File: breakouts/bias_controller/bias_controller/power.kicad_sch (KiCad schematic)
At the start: 9 parts, among them U7 LM2776

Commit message: top level schematic work
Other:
- note added: "add a few LEDs"
- moved on the sheet: C22, C23, C24, U7

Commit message: more bias controller schematic work
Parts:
- added C42, C43, C44: 4.7 uF, symbol Device:C_Small
- added R68: 20k, symbol Device:R_Small
- added R69: 0, symbol Device:R_Small
- added U18: LT3094xMSE, Package_SO:MSOP-12-1EP_3x4mm_P0.65mm_EP1.65x2.85mm, symbol Regulator_Linear:LT3094xMSE
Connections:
- net -6V: now also C42.1, U18.1 (IN), U18.13 (IN), U18.2 (IN), U18.3 (EN/UV), U18.5 (PGFB)
- net GND: now also C42.2, C43.2, C44.2, R68.1, U18.9 (GND)
- net VSS: now also C43.1, C44.1, R69.2, U18.10 (OUTS), U18.11 (OUT), U18.12 (OUT); no longer C25.1
- new net: R68.2, U18.6 (ILIM)
- new net VSS_EXT: C25.1, R69.1
- no-connect marks 0 -> 2
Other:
- note removed: "add negative ldo"
- moved on the sheet: C25, C26, R25, R26

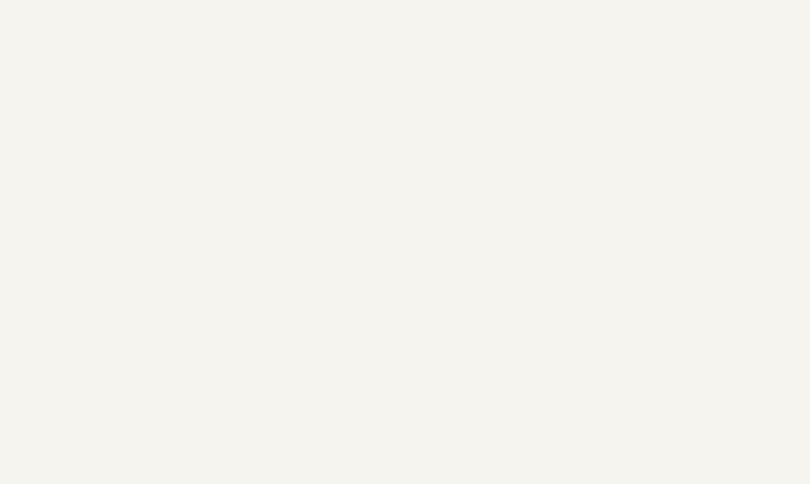
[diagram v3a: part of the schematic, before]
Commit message: added analog out op-amp circuits
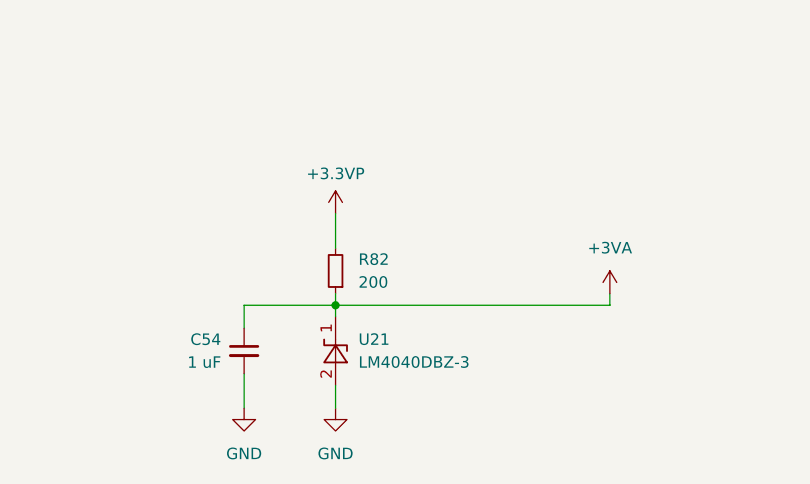
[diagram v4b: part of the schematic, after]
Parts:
- added C54: 1 uF, symbol Device:C_Small
- added R82: 200, symbol Device:R_Small
- added U21: LM4040DBZ-3, Package_TO_SOT_SMD:SOT-23, symbol Reference_Voltage:LM4040DBZ-3
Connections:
- net +3.3VP: now also R82.2
- net +3VA: now also C54.1, R82.1, U21.1 (K)
- net GND: now also C54.2, U21.2 (A)

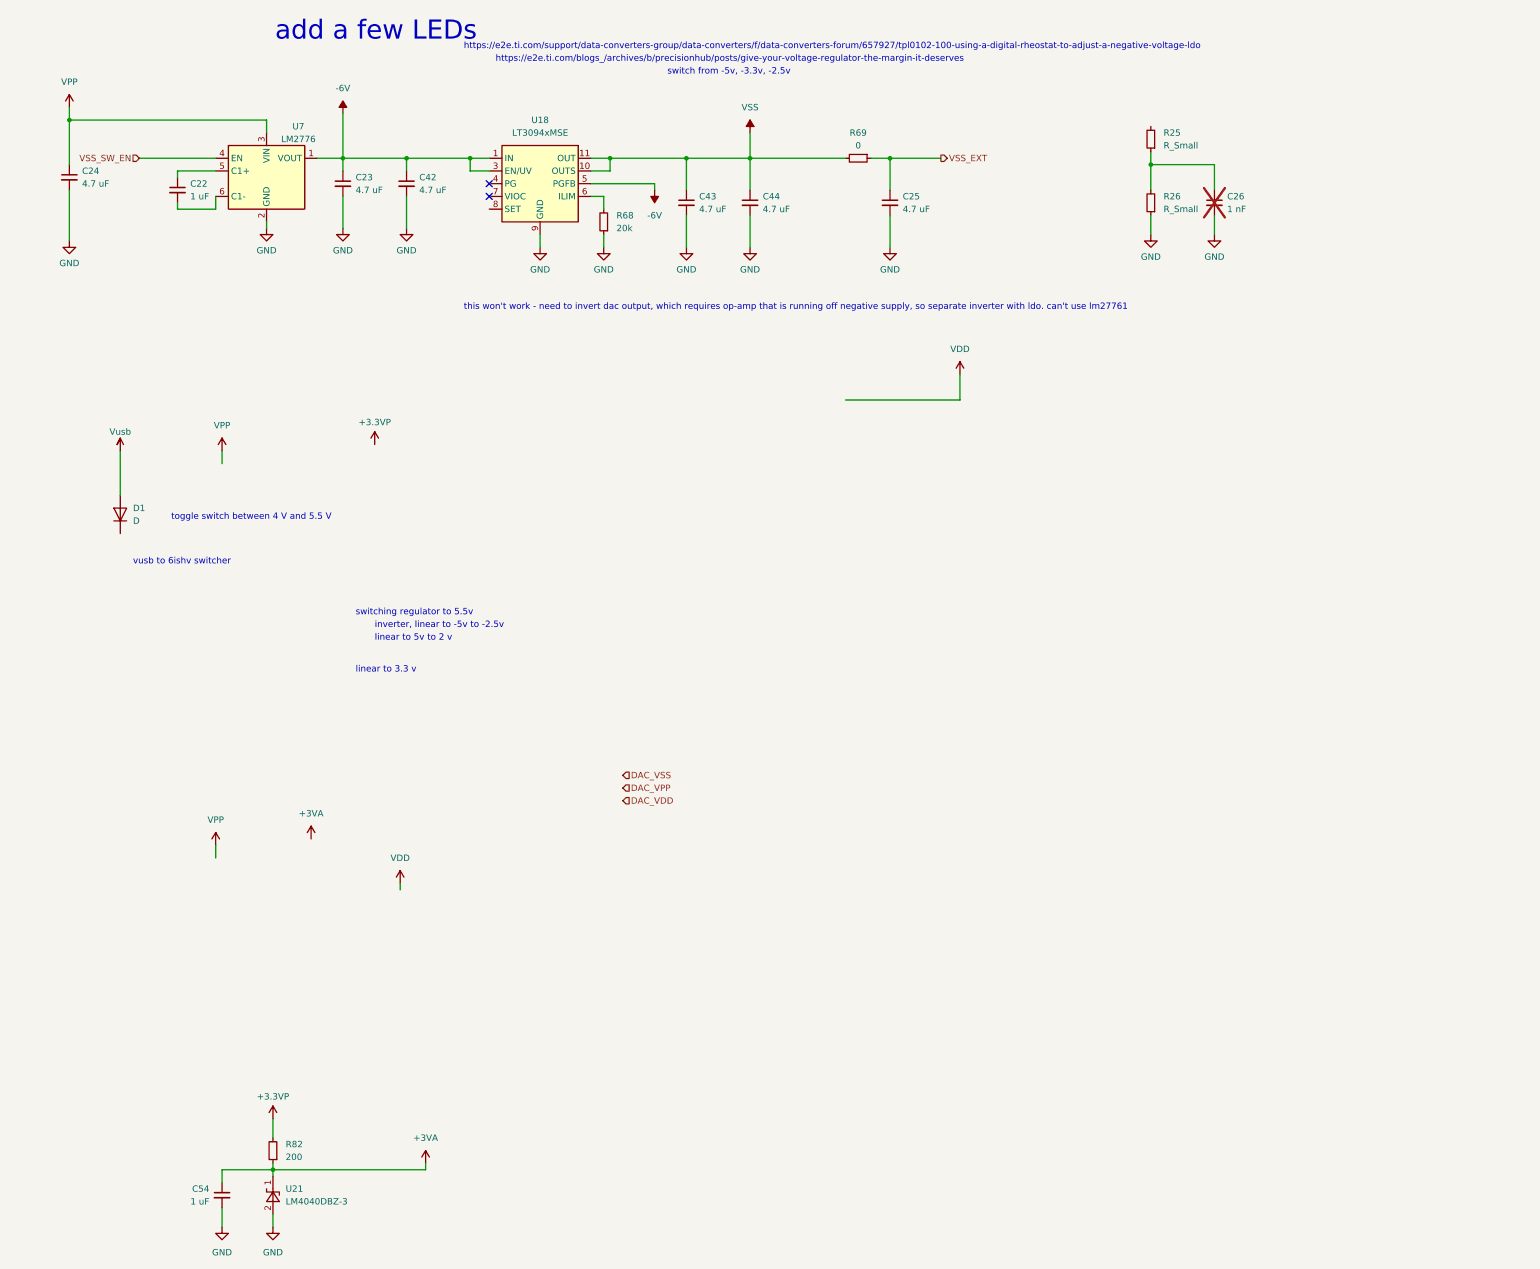
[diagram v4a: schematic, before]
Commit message: finished first pass at bias controller schematic
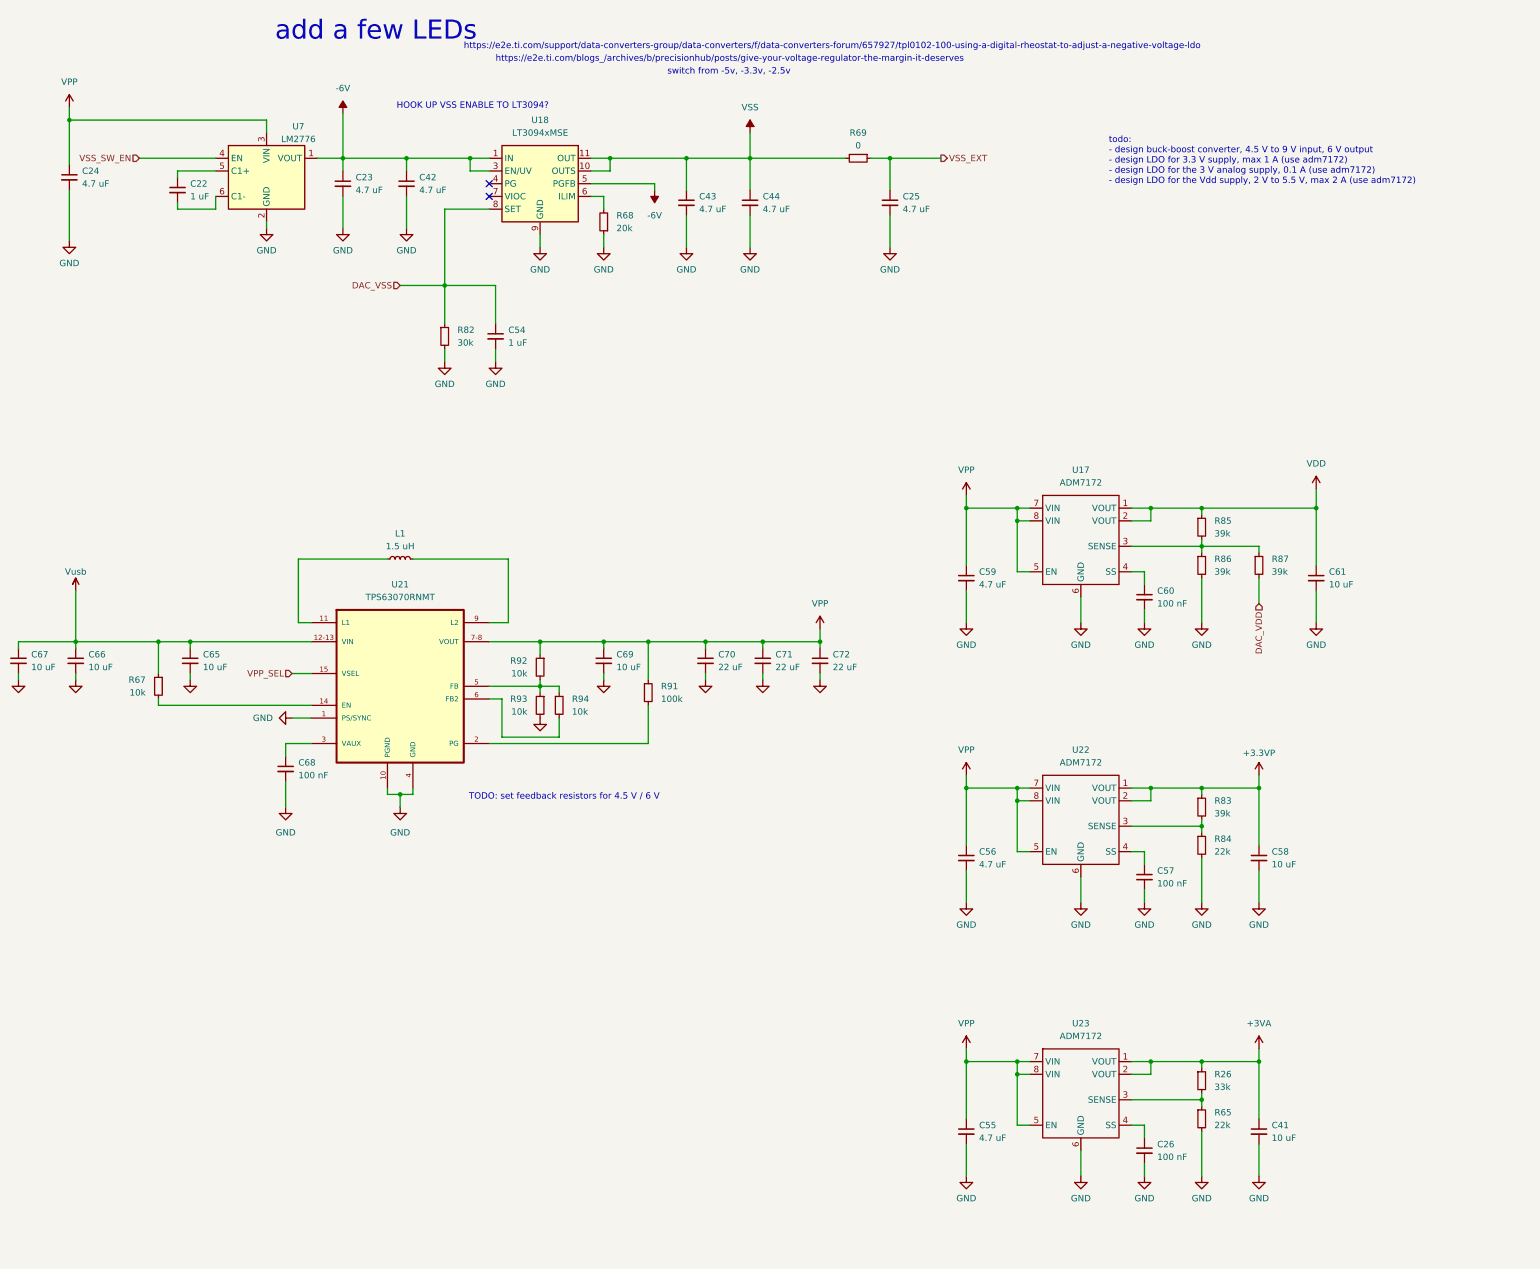
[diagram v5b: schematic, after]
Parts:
- removed D1: D, symbol Device:D
- removed R25: R_Small, symbol Device:R_Small
- removed U21: LM4040DBZ-3, Package_TO_SOT_SMD:SOT-23, symbol Reference_Voltage:LM4040DBZ-3
- added C41, C58, C61, C65, C66, C67, C69: 10 uF, symbol Device:C_Small
- added C55, C56, C59: 4.7 uF, symbol Device:C_Small
- added C57, C60, C68: 100 nF, symbol Device:C_Small
- added C70, C71, C72: 22 uF, symbol Device:C_Small
- added L1: 1.5 uH, symbol Device:L_Small
- added R65, R84: 22k, symbol Device:R_Small
- added R67, R92, R93, R94: 10k, symbol Device:R_Small
- added R83, R85, R86, R87: 39k, symbol Device:R_Small
- added R91: 100k, symbol Device:R_Small
- added U17, U22, U23: ADM7172, Package_CSP:LFCSP-8-1EP_3x3mm_P0.5mm_EP1.6x2.34mm, symbol jtk_rf:ADM7172
- added U21: TPS63070RNMT, snapeda:VREG_TPS63070RNMR, symbol tps63070:TPS63070RNMT
- C26: value 1 nF -> 100 nF; now fitted
- R26: value R_Small -> 33k
- R82: value 200 -> 30k
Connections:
- net +3.3VP: now also C58.1, R83.1, U22.1 (VOUT), U22.2 (VOUT); no longer R82.2
- net +3VA: now also R26.1, C41.1, U23.1 (VOUT), U23.2 (VOUT); no longer C54.1, R82.1
- net DAC_VDD: now also R87.2
- net DAC_VSS: now also C54.1, R82.1, U18.8 (SET)
- net GND: now also R82.2, C41.2, C55.2, C56.2, C57.2, C58.2, C59.2, C60.2, C61.2, C65.2, C66.2, C67.2, C68.2, C69.2, C70.2, C71.2, C72.2, R65.2, R84.2, R86.2, R93.2, U17.6 (GND), U17.9 (GND), U21.1 (PS/SYNC), U21.10 (PGND), U21.4 (GND), U22.6 (GND), U22.9 (GND), U23.6 (GND), U23.9 (GND); no longer R26.1
- net VDD: now also C61.1, R85.1, U17.1 (VOUT), U17.2 (VOUT)
- net VPP: now also C55.1, C56.1, C59.1, C69.1, C70.1, C71.1, C72.1, R91.1, R92.1, U17.5 (EN), U17.7 (VIN), U17.8 (VIN), U21.7-8 (VOUT), U22.5 (EN), U22.7 (VIN), U22.8 (VIN), U23.5 (EN), U23.7 (VIN), U23.8 (VIN)
- net Vusb: now also C65.1, C66.1, C67.1, R67.1, U21.12-13 (VIN)
- net at R26.2: now also R65.1, U23.3 (SENSE); no longer C26.1
- new net: R92.2, R93.1, R94.1, U21.5 (FB)
- new net: R94.2, U21.6 (FB2)
- new net: C68.1, U21.3 (VAUX)
- new net: R85.2, R86.1, R87.1, U17.3 (SENSE)
- new net: R83.2, R84.1, U22.3 (SENSE)
- new net: L1.1, U21.11 (L1)
- new net: L1.2, U21.9 (L2)
- new net: C60.1, U17.4 (SS)
- new net: C26.1, U23.4 (SS)
- new net: R67.2, U21.14 (EN)
- new net: C57.1, U22.4 (SS)
- new net: R91.2, U21.2 (PG)
- new net VPP_SEL: U21.15 (VSEL)
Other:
- note added: "HOOK UP VSS ENABLE TO LT3094?"
- note added: "TODO: set feedback resistors for 4.5 V / 6 V"
- note added: "todo: - design buck-boost converter, 4.5 V to 9 V input, 6 V output - design LDO for 3.3 V supply, max 1 A (use adm7172) - design LDO for the 3 V analog supply, 0.1 A (use adm7172) - design LDO for the Vdd supply, 2 V to 5.5 V, max 2 A (use adm7172)"
- note removed: "inverter, linear to -5v to -2.5v"
- note removed: "linear to 3.3 v"
- note removed: "linear to 5v to 2 v"
- note removed: "switching regulator to 5.5v"
- note removed: "this won't work - need to invert dac output, which requires op-amp that is running off negative supply, so separate inverter with ldo. can't use lm27761"
- note removed: "toggle switch between 4 V and 5.5 V"
- note removed: "vusb to 6ishv switcher"
